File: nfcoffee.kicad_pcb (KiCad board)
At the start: 2 copper layers, 36 x 58.5 mm, 17 parts, among them J1 Conn_Buzz, J3 Conn_SD_Shield_Left, J4 Conn_SD_Shiled_Right, J5 Conn_OLED, J6 Conn_PN532_NFC, Q1 BSS123, U1 WEMOS_D1_mini

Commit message: added SD card to PCB on the wrong layer
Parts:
- removed J3: Conn_SD_Shield_Left, Connector_PinSocket_2.54mm:PinSocket_1x08_P2.54mm_Vertical
- removed J4: Conn_SD_Shiled_Right, Connector_PinSocket_2.54mm:PinSocket_1x08_P2.54mm_Vertical
- added C1: 100nF, Capacitor_SMD:C_1206_3216Metric_Pad1.33x1.80mm_HandSolder, B.Cu at (51.8, 41.2)
- added MICRO_SD1: MICRO_SD(TFC-9P-1.xH(ATFFS150A01BR016)), olimex:J_SD_Card-micro_socket_A, F.Cu at (52.6, 42.9)
- J5: footprint Connector_PinHeader_2.54mm:PinHeader_1x04_P2.54mm_Vertical -> Connector_PinSocket_2.54mm:PinSocket_1x04_P2.54mm_Vertical
- J6: footprint Connector_PinHeader_2.54mm:PinHeader_1x08_P2.54mm_Vertical -> Connector_PinSocket_2.54mm:PinSocket_1x08_P2.54mm_Vertical
- R1, R2, R3, R4, R5, R6, R7, R8: value (none) -> R
- RD1: value 4k7 -> 10k
- RD2: value 10k -> 4k7
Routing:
- net 3V3: track 2.86 -> 20.4 mm, vias 0 -> 1
- net GPIO13: track 9.05 -> 18.4 mm, vias 0 -> 1
- net GPIO2: track 9.33 -> 16.1 mm, vias 0 -> 1
- net GPIO14: track 7.32 -> 12.6 mm, vias 0 -> 1
- net GPIO5: track 7.30 -> 4.28 mm
- net GPIO4: track 7.24 -> 4.22 mm
- net GND: track 3.65 -> 0.64 mm
- net GPIO0: track 7.87 -> 4.86 mm
- net GPIO15: track 2.86 -> 0.00 mm
- net GPIO12: track 8.24 -> 10.9 mm, vias 0 -> 1
- net PN532_MOSI: track 51.2 -> 51.7 mm
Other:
- board text added: "NFCoffee_v5"
- board text removed: "NFCoffee_v4"

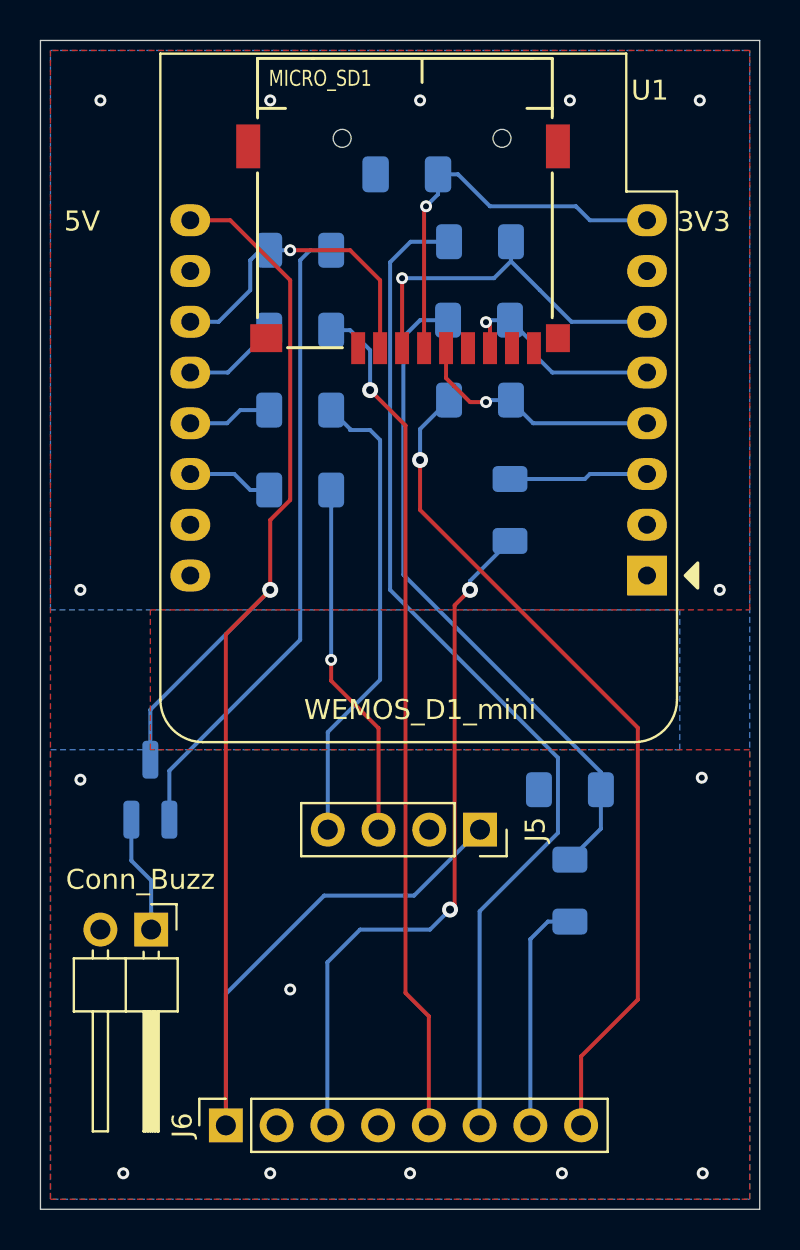
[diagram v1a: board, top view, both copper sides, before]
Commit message: Removed SD Shield and replaced with a SD Card Connector directly. Removed current limiting resistors.
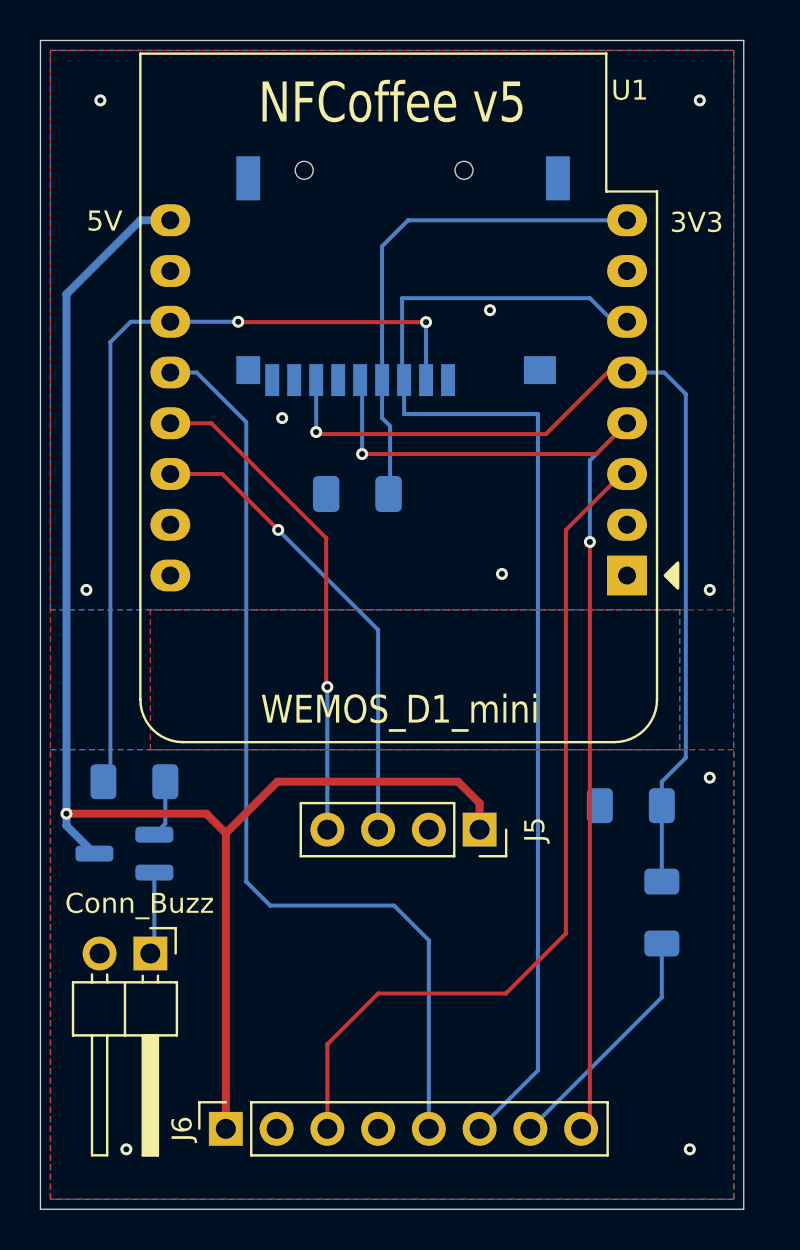
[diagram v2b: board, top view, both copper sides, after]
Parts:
- removed R1, R2, R3, R4, R5, R6, R7, R8: R, Resistor_SMD:R_1206_3216Metric_Pad1.30x1.75mm_HandSolder
- added RBuzz1: 1k, Resistor_SMD:R_1206_3216Metric_Pad1.30x1.75mm_HandSolder, B.Cu at (38.2, 71.6)
- MICRO_SD1: moved to B.Cu
- moved C1 16.2 mm to (49.4, 57.2)
- moved RD1 4.73 mm to (64.6, 78.2)
- moved Q1 3.45 mm to (37.7, 75.2), turned to 180 degrees
- moved RD2 3.15 mm to (63.0, 72.8)
- moved MICRO_SD1 2.51 mm to (50.7, 44.5), turned to 180 degrees
- moved J1 1.20 mm to (39.0, 80.2)
- moved U1 1.00 mm to (62.9, 61.3)
- moved J6 0.17 mm to (42.8, 89.0)
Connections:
- J5 pad 3: OLED_SCL -> GPIO5
- J5 pad 4: OLED_SDA -> GPIO4
- J6 pad 3: PN532_RST_D0 -> GPIO16
- J6 pad 5: PN532_CS -> GPIO0
- J6 pad 6: PN532_MOSI -> GPIO13
- J6 pad 8: PN532_SCLK -> GPIO14
- RD1 pad 2: RDx -> GPIO12
- RD2 pad 1: RDx -> GPIO12
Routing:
- net PN532_MOSI: track 51.7 -> 0.00 mm
- net GPIO13: track 18.4 -> 61.3 mm, vias 1 -> 0
- net GPIO0: track 4.86 -> 47.6 mm
- net PN532_SCLK: track 42.6 -> 0.00 mm, vias 1 -> 0
- net PN532_CS: track 42.4 -> 0.00 mm, vias 1 -> 0
- net GPIO14: track 12.6 -> 53.9 mm, vias 1 -> 2
- net GPIO12: track 10.9 -> 47.9 mm
- net GPIO16: track 6.96 -> 42.9 mm
- net PN532_RST_D0: track 35.1 -> 0.00 mm, vias 2 -> 0
- net RDx: track 33.5 -> 0.00 mm
- net Net-(Q1-G): track 32.5 -> 2.88 mm
- net GPIO2: track 16.1 -> 41.3 mm, vias 1 -> 2
- net OLED_SDA: track 23.7 -> 0.00 mm
- net GPIO4: track 4.22 -> 24.8 mm, vias 0 -> 1
- net GPIO5: track 4.28 -> 23.6 mm, vias 0 -> 1
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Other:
- board size 36 x 58.5 mm -> 35.2 x 58.5 mm
- board text added: "NFCoffee v5"
- board text removed: "NFCoffee_v5"

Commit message: Final changes on text after SD Card layout validation. Sent to JLC as v5.
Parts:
- J1: value Conn_Buzz -> Buzz
- J5: value Conn_OLED -> OLED
- J6: value Conn_PN532_NFC -> PN532_NFC
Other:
- board text added: "♥JLCPCB"

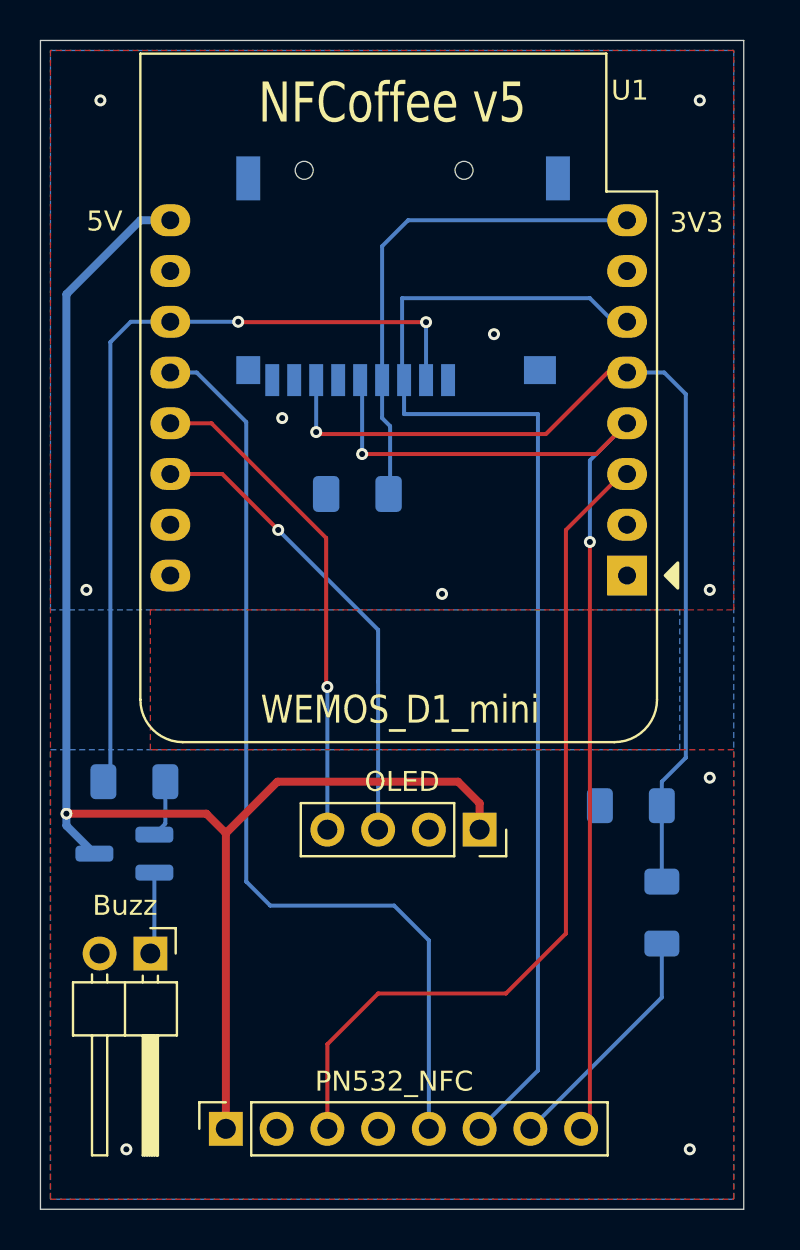
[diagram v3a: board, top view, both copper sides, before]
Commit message: Version 5.1 - fixed the connection for the SD card chipselect, moved to GPIO15; - added 22 ohm resistor at the start of SPI CLK line; -removed the voltage divisor for PN532 CIPO because the SPI works on 3V3 anyway; - connected the SPI lines in a chain (not star) topo. From ESP8266 to the SD card and then to the PN532; - added production files for JLCPCB generated by the JLCPCB plug-in; - added DRU file for JLCPCB.
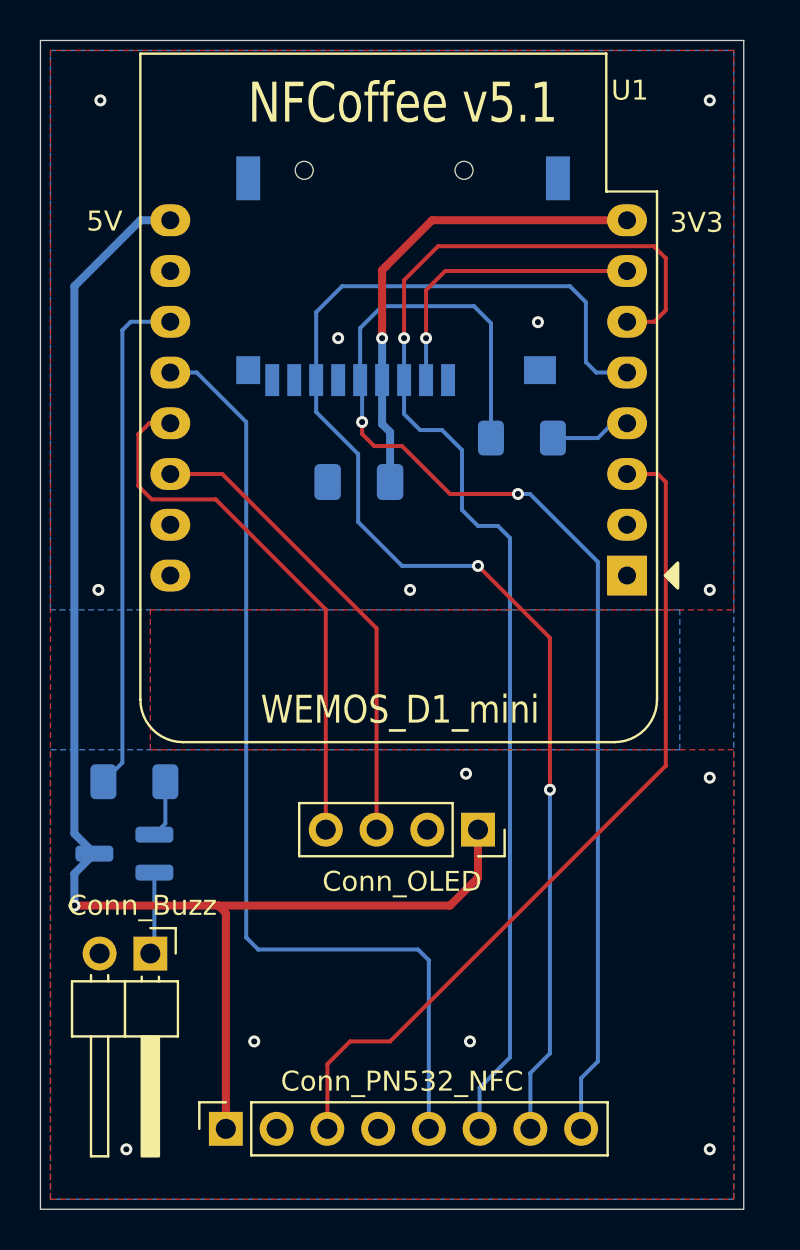
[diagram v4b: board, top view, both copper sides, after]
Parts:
- removed RD1: 10k, Resistor_SMD:R_1206_3216Metric_Pad1.30x1.75mm_HandSolder
- removed RD2: 4k7, Resistor_SMD:R_1206_3216Metric_Pad1.30x1.75mm_HandSolder
- added RSCK1: 22R, Resistor_SMD:R_1206_3216Metric_Pad1.30x1.75mm_HandSolder, B.Cu at (57.6, 54.4)
- J1: value Buzz -> Conn_Buzz
- J5: value OLED -> Conn_OLED
- J6: value PN532_NFC -> Conn_PN532_NFC
- RBuzz: renamed from RBuzz1; value 1k -> R
- moved C1 0.60 mm to (49.4, 56.6)
- moved J5 0.08 mm to (55.4, 74.0)
- renumbered MICRO_SD1 to MICRO_SD
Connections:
- J6 pad 7: PN532_MISO -> GPIO12
- MICRO_SD pad 2: GPIO2 -> GPIO15
- U1 pad 4: GPIO14 -> SCK
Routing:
- net GPIO12: track 47.9 -> 68.2 mm, vias 1 -> 2
- net GPIO2: track 41.3 -> 25.6 mm, vias 2 -> 0
- net GPIO15: track 0.00 -> 15.0 mm, vias 0 -> 1
- net PN532_MISO: track 12.0 -> 0.00 mm
- net GPIO14: track 53.9 -> 62.9 mm
- net SCK: track 0.00 -> 4.34 mm
- net GPIO13: track 61.3 -> 65.4 mm, vias 0 -> 1
- net GPIO4: track 24.8 -> 27.4 mm, vias 1 -> 0
- net 5V: track 74.0 -> 72.8 mm
- net GPIO0: track 47.6 -> 48.7 mm
- net 3V3: track 25.3 -> 24.6 mm, vias 0 -> 1
- net GPIO5: vias 1 -> 0
- net GND: vias 10 -> 13
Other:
- board text added: "NFCoffee v5.1"
- board text removed: "NFCoffee v5"
